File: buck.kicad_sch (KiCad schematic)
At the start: 21 parts, among them Q401 2N7002, U401 LM5169PDDAR

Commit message: added y cap and changed the inductor value, added simulator of pi filter
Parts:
- L402: footprint Inductor_SMD:L_Changjiang_FNR5040S -> Inductor_SMD:L_Changjiang_FTC252008S; LCSC C9389 -> C46961986

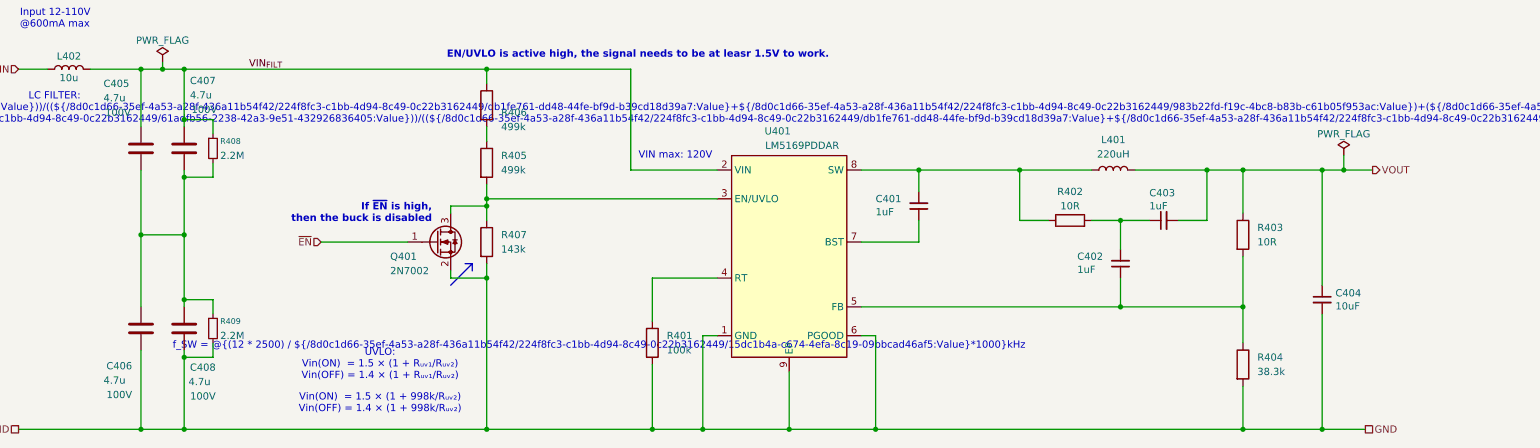
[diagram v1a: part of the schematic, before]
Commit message: Found IC for ORing function. Added all LCSC refs. Found proper header stackup.
Signed-off-by: Jean Alinei <jean.alinei@owntech.org>
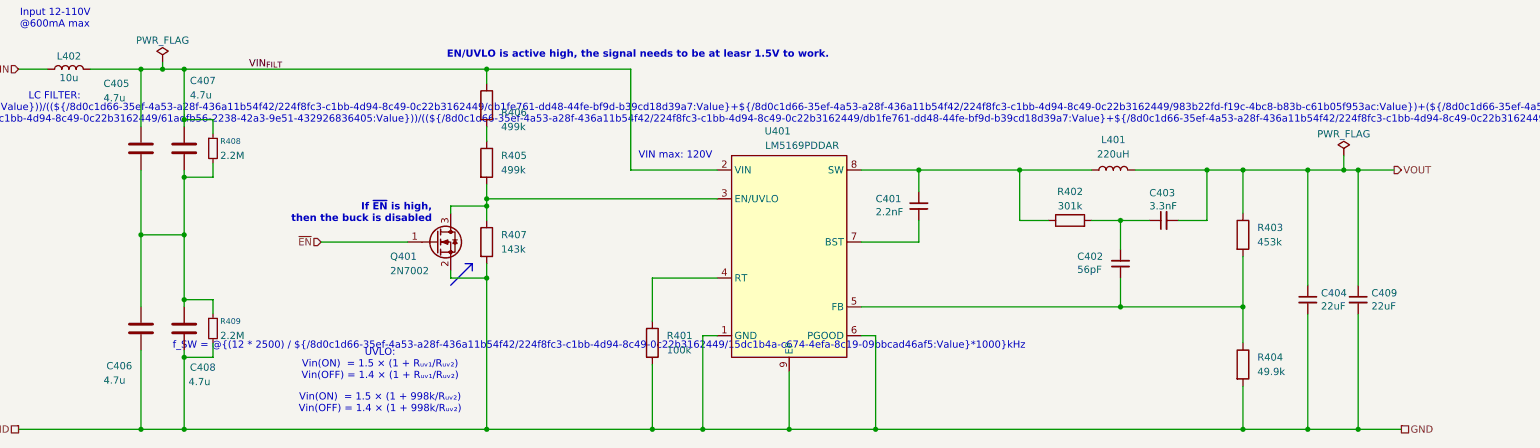
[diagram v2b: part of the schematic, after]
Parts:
- added C409: 22uF, Capacitor_SMD:C_0805_2012Metric, symbol Device:C_Small
- C401: value 1uF -> 2.2nF; LCSC (none) -> C28260; Reserved1 e9f2fe702f977b3e8607f4ffb8b8e4404782bd2b849b -> (none); manf# UMK212B7105KGHT -> (none)
- C402: value 1uF -> 56pF; LCSC (none) -> C1828; Reserved1 e9f2fe702f977b3e8607f4ffb8b8e4404782bd2b849b -> (none); manf# UMK212B7105KGHT -> (none)
- C403: value 1uF -> 3.3nF; LCSC (none) -> C77062; Reserved1 e9f2fe702f977b3e8607f4ffb8b8e4404782bd2b849b -> (none); manf# UMK212B7105KGHT -> (none)
- C404: value 10uF -> 22uF; footprint Footprints:C_1210_3225Metric -> Capacitor_SMD:C_0805_2012Metric; LCSC (none) -> C45783; Reserved1 6ef4274804797e6557917bb79bd82a607ad050021f56b2 -> (none); Voltage 50V -> (none); manf# 12105C106KAT2A -> (none)
- C405, C406, C407, C408: footprint Footprints:C_1210_3225Metric -> Capacitor_SMD:C_1206_3216Metric; LCSC (none) -> C22367839; Package 1210 -> (none); Reserved1 0db098cf967df37918c59b0e08ade59c874a0accb68a991e -> (none); Voltage 100V -> (none); manf# 12101C475K4T2A -> (none)
- R401: footprint Footprints:R_0805_2012Metric -> Resistor_SMD:R_0603_1608Metric; LCSC (none) -> C15458; Package 0805 -> (none); Reserved1 0033a278416cfa2b888d35575b40f177dfa85dffb5a098 -> (none); manf# CR0805-FX-1003ELF -> (none)
- R402: value 10R -> 301k; LCSC (none) -> C17619; Package 0805 -> (none); Reserved1 05fe8827ba2c4b813abe8e367446600b3e51597b2a0d -> (none); manf# CRCW080510R0JNEAC -> (none)
- R403: value 10R -> 453k; LCSC (none) -> C17702; Package 0805 -> (none); Reserved1 05fe8827ba2c4b813abe8e367446600b3e51597b2a0d -> (none); manf# CRCW080510R0JNEAC -> (none)
- R404: value 38.3k -> 49.9k; LCSC (none) -> C17719; Reserved1 5dc72b0eab839e46b614cc49d68cfb4a88fb1d7b5f838a -> (none); manf# CRCW080538K3FKEA -> (none)
- R405, R406: LCSC (none) -> C17721; Package 0805 -> (none); Reserved1 0033a278416cfa2b888d35575b40f177dfa85dffb5a098 -> (none); manf# CR0805-FX-1003ELF -> (none)
- R407: LCSC (none) -> C247044; Package 0805 -> (none); Reserved1 0033a278416cfa2b888d35575b40f177dfa85dffb5a098 -> (none); manf# CR0805-FX-1003ELF -> (none)
- R408, R409: LCSC (none) -> C22356574
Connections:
- net GND: now also C409.2
- net VOUT: now also C409.1
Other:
- moved on the sheet: C404

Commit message: Added rotation offsets.
Signed-off-by: Jean Alinei <jean.alinei@owntech.org>
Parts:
- U401: Rotation Offset (none) -> 270
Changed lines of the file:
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@@
+			)
+		)
+		(property "Rotation Offset" "270"
+			(at 162.56 91.44 0)
+			(hide yes)
+			(show_name no)
+			(do_not_autoplace no)
+			(effects
+				(font
+					(size 1.27 1.27)
+				)
 			)
 		)
